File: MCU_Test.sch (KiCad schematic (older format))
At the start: 18 parts, among them U2 STM32F051K6Ux

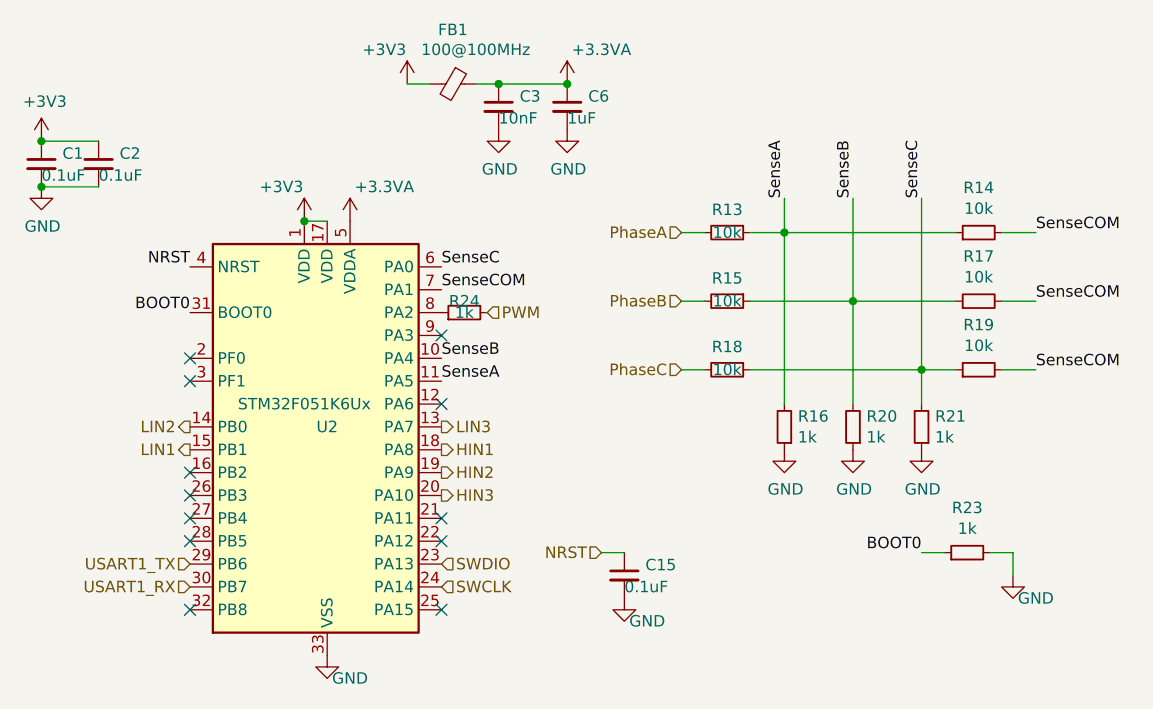
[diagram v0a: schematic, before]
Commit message: Added a test circuit to figure out best configuration
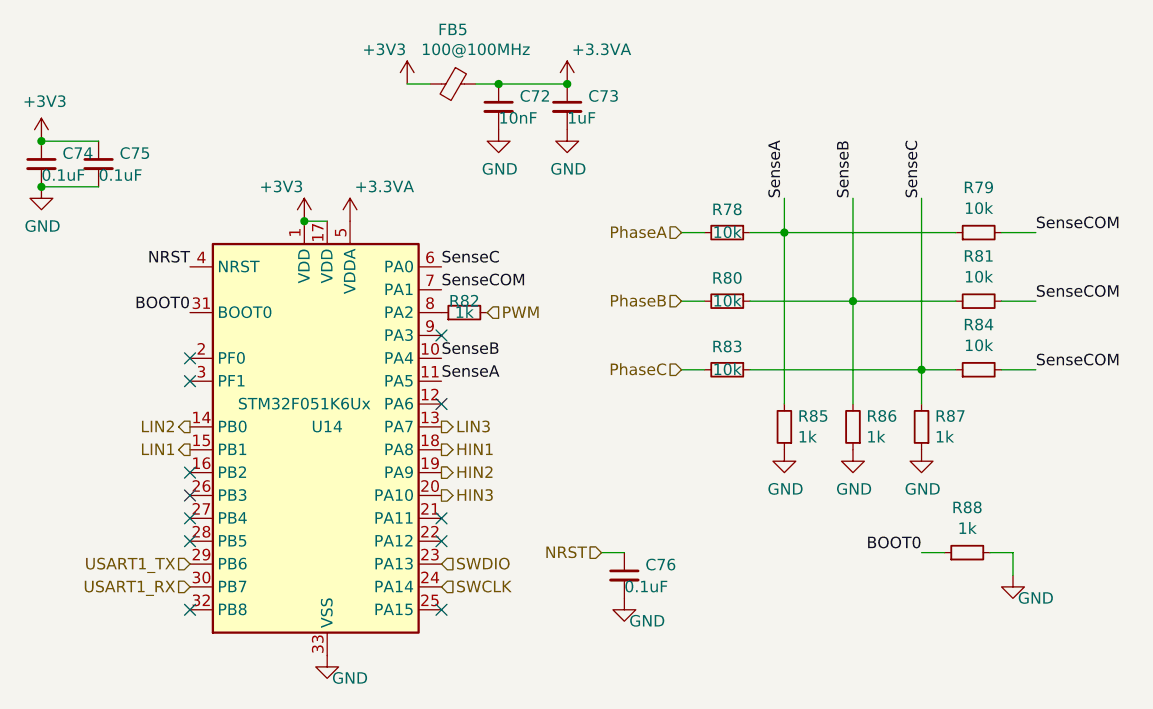
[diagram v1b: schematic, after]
